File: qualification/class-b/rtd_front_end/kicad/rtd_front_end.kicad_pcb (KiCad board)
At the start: 2 copper layers, 27 x 23.8 mm, 12 parts, among them U1 LM358

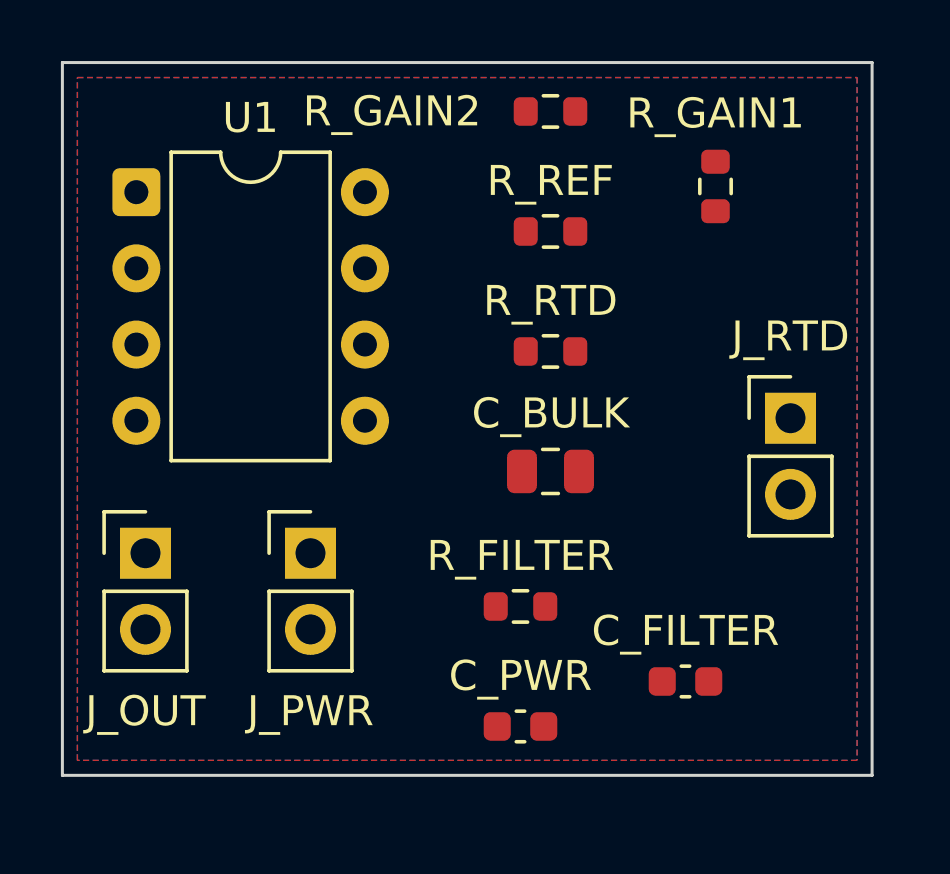
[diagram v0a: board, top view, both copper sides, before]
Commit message: fix: address PR review - restructure as qualification boards, fix RTD topology, USB ESD, BME280 (SYN-365)
Changes:
- Move from examples/ to qualification/class-b/<board>/ with README, SHA256SUMS, qualification.json
- Fix RTD amplifier: non-inverting gain stage (1+R2/R1=11x) instead of inverting
- Fix USB ESD: separate D_ESD_DP and D_ESD_DN diodes instead of shorting D+/D-
- Add BME280 part to registry (issue specifies BME280, not BME680)
- Add i2c_sda/i2c_scl capabilities to nrf52840 p0_06/p0_08
- Fix balun_2g4 footprint to real KiCad part
- Re-route BLE node: 0 unconnected pads (manual via-in-pad escape)
- Add DRC/ERC reports, SHA256SUMS, qualification.json for both boards
- Remove silkscreen labels, add USB-C 3D model reference
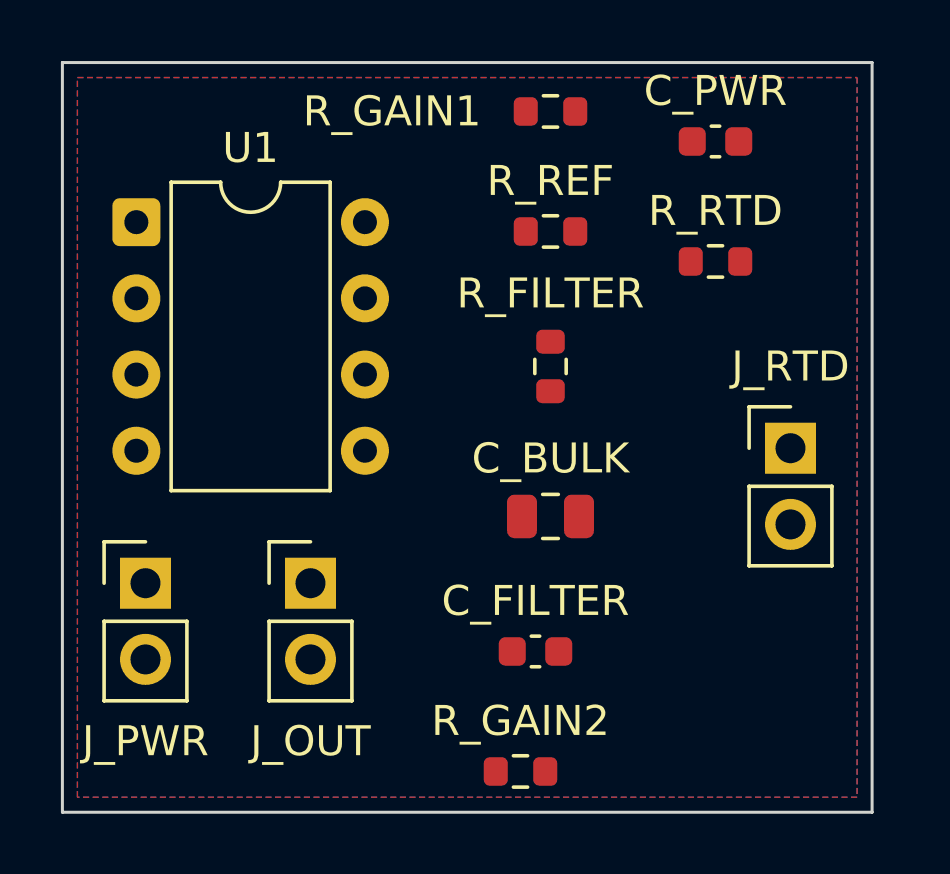
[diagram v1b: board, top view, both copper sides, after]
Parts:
- moved R_GAIN2 22.0 mm to (15.3, 23.7)
- moved C_PWR 20.6 mm to (21.8, 2.73)
- moved R_FILTER 8.06 mm to (16.3, 10.2), turned to 270 degrees
- moved R_RTD 6.26 mm to (21.8, 6.73)
- moved R_GAIN1 6.04 mm to (16.3, 1.73), turned to 0 degrees
- moved J_OUT 5.59 mm to (8.27, 17.5)
- moved J_PWR 5.59 mm to (2.77, 17.5)
- moved C_FILTER 5.10 mm to (15.8, 19.7)
- moved C_BULK 1.50 mm to (16.3, 15.2)
- moved J_RTD 1.00 mm to (24.3, 13.0)
- moved U1 1.00 mm to (2.46, 5.42)
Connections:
- R_GAIN1 pad 1: net_3 -> net_4
- R_GAIN1 pad 2: net_4 -> GND
- U1 pad 5: GND -> net_3
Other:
- board size 27 x 23.8 mm -> 27 x 25 mm
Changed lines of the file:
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@@
 	(gr_line
 		(start 26.99 0.1)
-		(end 26.99 23.86)
+		(end 26.99 25.09)
 		(stroke
 			(width 0.1)
@@
 	)
 	(gr_line
-		(start 26.99 23.86)
-		(end 0 23.86)
+		(start 26.99 25.09)
+		(end 0 25.09)
 		(stroke
 			(width 0.1)
@@
 	)
 	(gr_line
-		(start 0 23.86)
+		(start 0 25.09)
 		(end 0 0.1)
 		(stroke
@@
 		"Connector_PinHeader_2.54mm:PinHeader_1x02_P2.54mm_Vertical"
 		(layer "F.Cu")
-		(at 8.27 16.455)
+		(at 2.77 17.455)
 		(property
 			"Reference"
@@
 		"Capacitor_SMD:C_0603_1608Metric"
 		(layer "F.Cu")
-		(at 15.27 22.23)
+		(at 21.77 2.73)
 		(property
 			"Reference"
@@
 		"Capacitor_SMD:C_0805_2012Metric"
 		(layer "F.Cu")
-		(at 16.27 13.73)
+		(at 16.27 15.23)
 		(property
 			"Reference"
@@
 		"Connector_PinHeader_2.54mm:PinHeader_1x02_P2.54mm_Vertical"
 		(layer "F.Cu")
-		(at 24.27 11.955)
+		(at 24.27 12.955)
 		(property
 			"Reference"
@@
 		"Resistor_SMD:R_0603_1608Metric"
 		(layer "F.Cu")
-		(at 16.27 9.73)
+		(at 21.77 6.73)
 		(property
 			"Reference"
@@
 		"Package_DIP:DIP-8_W7.62mm"
 		(layer "F.Cu")
-		(at 2.465 4.42)
+		(at 2.465 5.42)
 		(property
 			"Reference"
@@
 		(layers "*.Cu" "*.Mask")
 		(remove_unused_layers no)
-			(net 2 "GND")
+			(net 4 "net_3")
 )
 	(pad "6" thru_hole circle
@@
 		"Resistor_SMD:R_0603_1608Metric"
 		(layer "F.Cu")
-		(at 21.77 4.23 90)
+		(at 16.27 1.73)
 		(property
 			"Reference"
 			"R_GAIN1"
-			(at 2.43 0 0)
+			(at -5.28 0 0)
 			(layer "F.SilkS")
 			(effects
@@
 			"Value"
 			"10k"
-			(at 4.98 0 -90)
-			(layer "F.Fab")
-			(hide yes)
-			(effects
-				(font
-					(size 1 1)
-				)
-			)
-		)
-		(property
-			"Datasheet"
-			""
-			(at 0 0 0)
-			(layer "F.Fab")
-			(hide yes)
-			(effects
-				(font
-					(size 1.27 1.27)
-				)
-			)
-		)
-		(property
-			"Description"
-			""
-			(at 0 0 0)
-			(layer "F.Fab")
-			(hide yes)
-			(effects
-				(font
-					(size 1.27 1.27)
-				)
-			)
-		)
-		(property
-			"MPN"
-			""
-			(at 0 0 0)
-			(layer "F.Fab")
-			(hide yes)
-			(effects
-				(font
-					(size 1.27 1.27)
-				)
-			)
-		)
-		(property
-			"LCSC"
-			""
-			(at 0 0 0)
-			(layer "F.Fab")
-			(hide yes)
-			(effects
-				(font
-					(size 1.27 1.27)
-				)
-			)
-		)
-	(property "KiLib_Generator" "SMD_2terminal_chip_molded"
-		(at 0 0 0)
-		(layer "F.SilkS")
-		(hide yes)
-		(effects
-			(font
-				(size 1 1)
-				(thickness 0.15)
-			)
-		)
-)
-	(attr smd)
-	(duplicate_pad_numbers_are_jumpers no)
-	(fp_line
-		(start -0.237258 -0.5225)
-		(end 0.237258 -0.5225)
-		(stroke
-			(width 0.12)
-			(type solid)
-		)
-		(layer "F.SilkS")
-)
-	(fp_line
-		(start -0.237258 0.5225)
-		(end 0.237258 0.5225)
-		(stroke
-			(width 0.12)
-			(type solid)
-		)
-		(layer "F.SilkS")
-)
-	(fp_rect
-		(start -1.48 -0.73)
-		(end 1.48 0.73)
-		(stroke
-			(width 0.05)
-			(type solid)
-		)
-		(fill no)
-		(layer "F.CrtYd")
-)
-	(fp_rect
-		(start -0.8 -0.4125)
-		(end 0.8 0.4125)
-		(stroke
-			(width 0.1)
-			(type solid)
-		)
-		(fill no)
-		(layer "F.Fab")
-)
-	(pad "1" smd roundrect
-		(at -0.825 0 90)
-		(size 0.8 0.95)
-		(layers "F.Cu" "F.Mask" "F.Paste")
-		(roundrect_rratio 0.25)
-			(net 4 "net_3")
-)
-	(pad "2" smd roundrect
-		(at 0.825 0 90)
-		(size 0.8 0.95)
-		(layers "F.Cu" "F.Mask" "F.Paste")
-		(roundrect_rratio 0.25)
-			(net 5 "net_4")
-)
-	(embedded_fonts no)
-	(model "/usr/share/kicad/3dmodels/Resistor_SMD.3dshapes/R_0603_1608Metric.step"
-		(offset
-			(xyz 0 0 0)
-		)
-		(scale
-			(xyz 1 1 1)
-		)
-		(rotate
-			(xyz 0 0 0)
-		)
-	)
-	)
-	(footprint
-		"Resistor_SMD:R_0603_1608Metric"
-		(layer "F.Cu")
-		(at 16.27 1.73)
-		(property
-			"Reference"
-			"R_GAIN2"
-			(at -5.28 0 0)
-			(layer "F.SilkS")
-			(effects
-				(font
-					(size 1 1)
-				)
-			)
-		)
-		(property
-			"Value"
-			"100k"
 			(at 0 4.23 0)
 			(layer "F.Fab")
@@
 		(layers "F.Cu" "F.Mask" "F.Paste")
 		(roundrect_rratio 0.25)
-			(net 6 "net_5")
+			(net 2 "GND")
 )
 	(embedded_fonts no)
@@
 	)
 	(footprint
+		"Resistor_SMD:R_0603_1608Metric"
+		(layer "F.Cu")
+		(at 15.27 23.73)
+		(property
+			"Reference"
+			"R_GAIN2"
+			(at 0 -1.68 0)
+			(layer "F.SilkS")
+			(effects
+				(font
+					(size 1 1)
+				)
+			)
+		)
+		(property
+			"Value"
+			"100k"
+			(at 0 4.23 0)
+			(layer "F.Fab")
+			(hide yes)
+			(effects
+				(font
+					(size 1 1)
+				)
+			)
+		)
+		(property
+			"Datasheet"
+			""
+			(at 0 0 0)
+			(layer "F.Fab")
+			(hide yes)
+			(effects
+				(font
+					(size 1.27 1.27)
+				)
+			)
+		)
+		(property
+			"Description"
+			""
+			(at 0 0 0)
+			(layer "F.Fab")
+			(hide yes)
+			(effects
+				(font
+					(size 1.27 1.27)
+				)
+			)
+		)
+		(property
+			"MPN"
+			""
+			(at 0 0 0)
+			(layer "F.Fab")
+			(hide yes)
+			(effects
+				(font
+					(size 1.27 1.27)
+				)
+			)
+		)
+		(property
+			"LCSC"
+			""
+			(at 0 0 0)
+			(layer "F.Fab")
+			(hide yes)
+			(effects
+				(font
+					(size 1.27 1.27)
+				)
+			)
+		)
+	(property "KiLib_Generator" "SMD_2terminal_chip_molded"
+		(at 0 0 0)
+		(layer "F.SilkS")
+		(hide yes)
+		(effects
+			(font
+				(size 1 1)
+				(thickness 0.15)
+			)
+		)
+)
+	(attr smd)
+	(duplicate_pad_numbers_are_jumpers no)
+	(fp_line
+		(start -0.237258 -0.5225)
+		(end 0.237258 -0.5225)
+		(stroke
+			(width 0.12)
+			(type solid)
+		)
+		(layer "F.SilkS")
+)
+	(fp_line
+		(start -0.237258 0.5225)
+		(end 0.237258 0.5225)
+		(stroke
+			(width 0.12)
+			(type solid)
+		)
+		(layer "F.SilkS")
+)
+	(fp_rect
+		(start -1.48 -0.73)
+		(end 1.48 0.73)
+		(stroke
+			(width 0.05)
+			(type solid)
+		)
+		(fill no)
+		(layer "F.CrtYd")
+)
+	(fp_rect
+		(start -0.8 -0.4125)
+		(end 0.8 0.4125)
+		(stroke
+			(width 0.1)
+			(type solid)
+		)
+		(fill no)
+		(layer "F.Fab")
+)
+	(pad "1" smd roundrect
+		(at -0.825 0)
+		(size 0.8 0.95)
+		(layers "F.Cu" "F.Mask" "F.Paste")
+		(roundrect_rratio 0.25)
+			(net 5 "net_4")
+)
+	(pad "2" smd roundrect
+		(at 0.825 0)
+		(size 0.8 0.95)
+		(layers "F.Cu" "F.Mask" "F.Paste")
+		(roundrect_rratio 0.25)
+			(net 6 "net_5")
+)
+	(embedded_fonts no)
+	(model "/usr/share/kicad/3dmodels/Resistor_SMD.3dshapes/R_0603_1608Metric.step"
+		(offset
+			(xyz 0 0 0)
+		)
+		(scale
+			(xyz 1 1 1)
+		)
+		(rotate
+			(xyz 0 0 0)
+		)
+	)
+	)
+	(footprint
 		"Capacitor_SMD:C_0603_1608Metric"
 		(layer "F.Cu")
-		(at 20.77 20.73)
+		(at 15.77 19.73)
 		(property
 			"Reference"
@@
 		"Resistor_SMD:R_0603_1608Metric"
 		(layer "F.Cu")
-		(at 15.27 18.23)
+		(at 16.27 10.23 270)
 		(property
 			"Reference"
 			"R_FILTER"
-			(at 0 -1.68 0)
+			(at -2.43 0 0)
 			(layer "F.SilkS")
 			(effects
@@
 			"Value"
 			"10k"
-			(at 0 4.23 0)
+			(at -4.98 0 90)
 			(layer "F.Fab")
 			(hide yes)
@@
 )
 	(pad "1" smd roundrect
-		(at -0.825 0)
+		(at -0.825 0 270)
 		(size 0.8 0.95)
 		(layers "F.Cu" "F.Mask" "F.Paste")
@@
 )
 	(pad "2" smd roundrect
-		(at 0.825 0)
+		(at 0.825 0 270)
 		(size 0.8 0.95)
 		(layers "F.Cu" "F.Mask" "F.Paste")
@@
 		"Connector_PinHeader_2.54mm:PinHeader_1x02_P2.54mm_Vertical"
 		(layer "F.Cu")
-		(at 2.77 16.455)
+		(at 8.27 17.455)
 		(property
 			"Reference"
@@
 				(xy 0.5 0.6)
 				(xy 26.49 0.6)
-				(xy 26.49 23.36)
-				(xy 0.5 23.36)
+				(xy 26.49 24.59)
+				(xy 0.5 24.59)
 			)
 		)
@@
 				(xy 0.5 0.6)
 				(xy 26.49 0.6)
-				(xy 26.49 23.36)
-				(xy 0.5 23.36)
-			)
-		)
+				(xy 26.49 24.59)
+				(xy 0.5 24.59)
+			)
+		)

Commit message: fix: address PR review #3 - clean DRC, fix RTD topology, update evidence (SYN-365)
- BLE DRC: 0 unconnected pads, 6 violations (2 silk_over_copper warnings, 2 hole_clearance, 2 clearance) - all from manual escape segments
- RTD DRC: 0 unconnected pads, 4 violations (all silkscreen warnings, 0 electrical)
- RTD ERC: 0 errors (removed +3V3 power declaration that caused false positive)
- Fixed RTD topology: removed shunt resistor, external RTD connects via J_RTD
- Fixed RTD gain: 5x (was 11x, exceeded 3.3V output range)
- Fixed CI lint: clone_from instead of clone in island_vias.rs
- Updated qualification.json with honest DRC/ERC status
- Regenerated SHA256SUMS and DRC reports
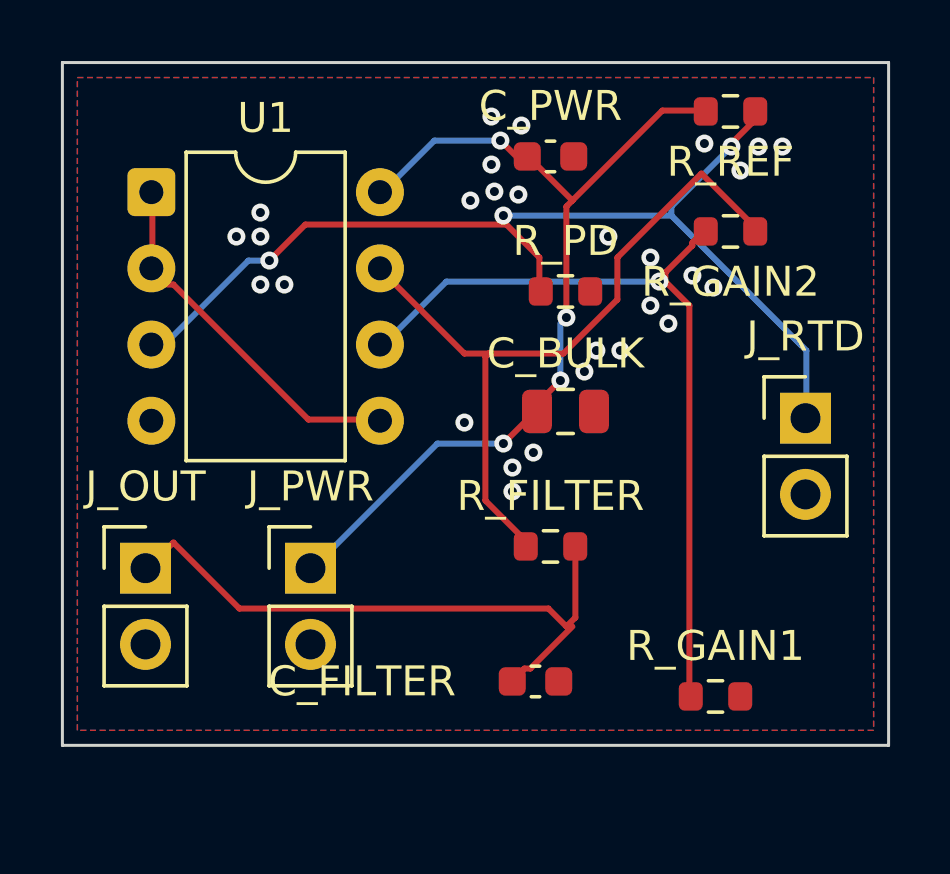
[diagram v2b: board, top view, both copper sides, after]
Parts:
- removed R_RTD: 100, Resistor_SMD:R_0603_1608Metric
- added R_PD: 100k, Resistor_SMD:R_0603_1608Metric, F.Cu at (16.8, 7.73)
- R_GAIN2: value 100k -> 40k
- moved R_GAIN1 20.3 mm to (21.8, 21.2)
- moved R_GAIN2 19.3 mm to (22.3, 5.73)
- moved R_REF 7.21 mm to (22.3, 1.73)
- moved R_FILTER 6.00 mm to (16.3, 16.2), turned to 0 degrees
- moved C_PWR 5.52 mm to (16.3, 3.23)
- moved J_OUT 5.52 mm to (2.77, 17.0)
- moved J_PWR 5.52 mm to (8.27, 17.0)
- moved C_BULK 3.54 mm to (16.8, 11.7)
- moved J_RTD 1.12 mm to (24.8, 12.0)
- moved U1 1.12 mm to (2.96, 4.42)
- moved C_FILTER 1.00 mm to (15.8, 20.7)
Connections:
- net +3V3 renamed net_0
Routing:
- net net_2: track 0.00 -> 34.1 mm, vias 0 -> 3
- net net_0: track 0.00 -> 29.9 mm, vias 0 -> 4
- net net_4: track 0.00 -> 26.4 mm, vias 0 -> 1
- net net_5: track 0.00 -> 24.5 mm
- net net_6: track 0.00 -> 21.2 mm
- net net_3: track 0.00 -> 11.6 mm
- net 3: vias 0 -> 12
- net 2: vias 0 -> 9
- net 1: vias 0 -> 7
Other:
- board size 27 x 25 mm -> 27.5 x 22.8 mm
- net class Default removed
- net class Power removed
